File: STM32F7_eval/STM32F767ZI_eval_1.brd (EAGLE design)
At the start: 76.2 x 53.3 mm, 103 parts, among them CN1 STLINKV2_SWD_IF_, CN2 GROVE-4P-CONN-I2C-90D, CN3 GROVE-4P-CONN-I2C-90D, CN5 ARDUINO_COMPAT_IF, CN7 WFT0750CZ09-SMD_, Q1 PMF370XN_, SW1 SKRPACE010_, SW2 SKRPACE010_, U1 STM32F767ZI_, U2 LD39050PU33R_DEV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

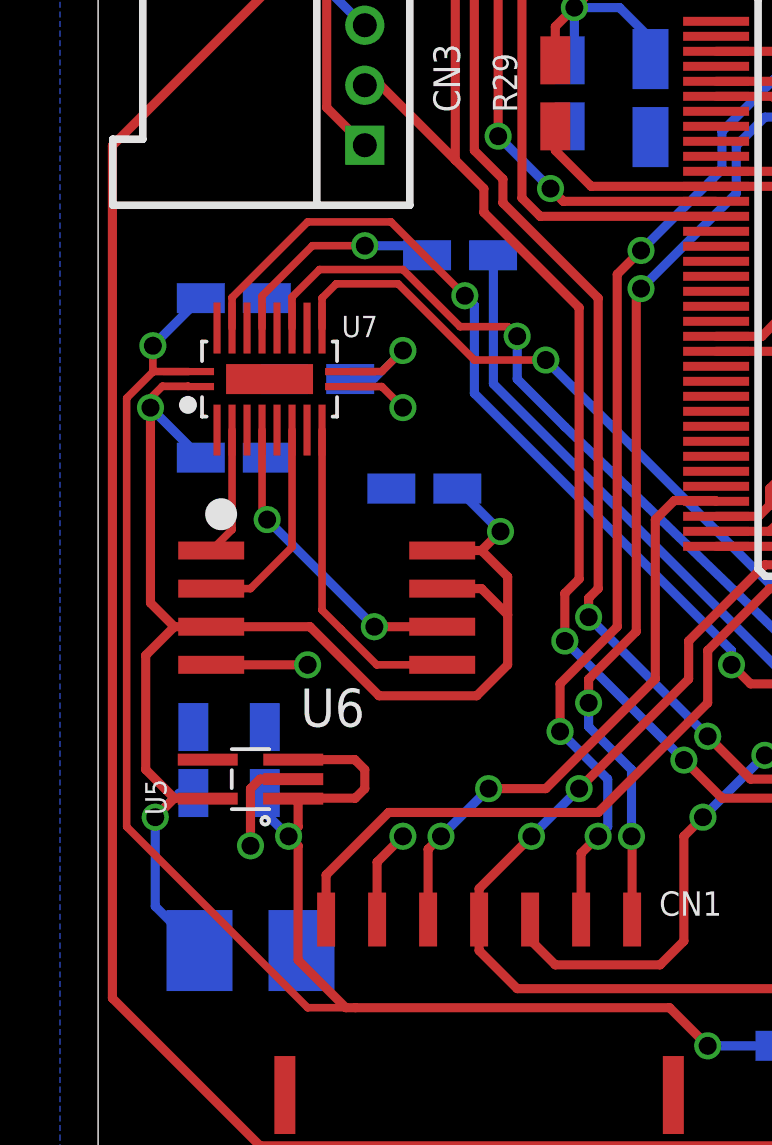
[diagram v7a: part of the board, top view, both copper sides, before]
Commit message: レイアウトを修正
・近接していた部品を移動
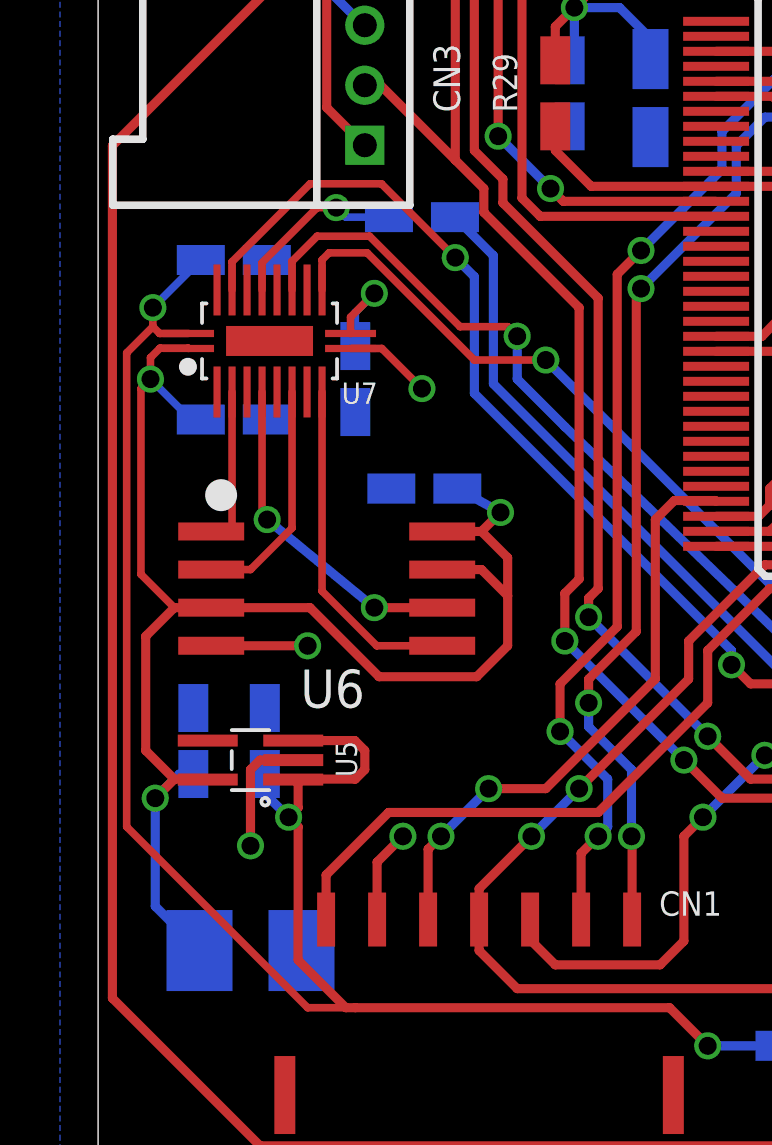
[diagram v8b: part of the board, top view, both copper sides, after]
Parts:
- moved R19 1.80 mm to (10.8, 31.4)
- moved C45 1.27 mm to (4.52, 24.7)
- moved C46 1.27 mm to (4.52, 30.0)
- moved R5 1.27 mm to (8.57, 26.0), turned to 90 degrees
- moved U7 1.27 mm to (5.71, 27.3)
- moved U5 0.64 mm to (5.08, 13.3)
- moved U6 0.64 mm to (7.62, 19.1)
- moved C42 0.63 mm to (3.17, 14.0)
- moved C49 0.63 mm to (5.56, 14.0)
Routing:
- net VCC_MEM: track 60.4 -> 62.3 mm
- net PC10: track 22.5 -> 24.3 mm
- net 0V: track 171.5 -> 173.1 mm
- net PC10_D: track 7.39 -> 6.03 mm
- net +1V8: track 50.7 -> 51.8 mm
- net PA15: track 31.4 -> 32.4 mm
- net !CS!: track 4.30 -> 5.29 mm
- net SCLK: track 10.4 -> 11.2 mm
- net SO: track 7.17 -> 7.80 mm
- net SI: track 10.8 -> 11.4 mm
- net !OE!: track 4.19 -> 3.69 mm
